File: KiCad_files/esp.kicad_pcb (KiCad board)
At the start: 2 copper layers, 100 x 100 mm, 61 parts, among them J1 Conn_01x08_Socket, J2 USB4105-GF-A, Q2 DMP3099L, SW1 SLW-171175-7A-N-D, U1 B3U-1000P, U12 ESP32-S3-MINI-1U, U13 BNO085, U2 1060, U7 LTC4412xS6

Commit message: gepsiä alotettu
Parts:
- added J3: Conn_01x16_Pin, Connector_PinHeader_2.54mm:PinHeader_1x16_P2.54mm_Vertical, F.Cu at (48.2, 48.5)
- added TP1: BOOT, TestPoint:TestPoint_Pad_D1.0mm, F.Cu at (134.9, 58.9)
- added TP2: JTAG_SOURCE, TestPoint:TestPoint_Pad_D1.0mm, F.Cu at (134.9, 55.4)
- added TP3: VDD_SPI_VOLTAGE, TestPoint:TestPoint_Pad_D1.0mm, F.Cu at (100.0, 60.5)
- added TP4: ROM_PRINTING, TestPoint:TestPoint_Pad_D1.0mm, F.Cu at (100.0, 63.5)
- J1: value Conn_01x08_Socket -> Conn_01x02_Pin; footprint Connector_PinSocket_2.54mm:PinSocket_1x08_P2.54mm_Vertical -> Connector_PinHeader_2.54mm:PinHeader_1x02_P2.54mm_Vertical
- moved J2 79.2 mm to (80.6, 51.3), turned to -90 degrees
- moved R18 57.8 mm to (142.4, 58.6), turned to 90 degrees
- moved R17 57.0 mm to (139.9, 57.4), turned to 90 degrees
- moved C12 54.9 mm to (137.9, 32.3)
- moved C13 54.5 mm to (137.9, 35.8)
- moved C14 54.3 mm to (117.9, 30.1), turned to -90 degrees
- moved R9 50.4 mm to (116.4, 26.3)
- moved L3 48.3 mm to (133.9, 26.3)
- moved U10 43.5 mm to (125.2, 32.1)
- moved J1 42.9 mm to (124.5, 89.8)
- moved C11 42.2 mm to (116.9, 33.3), turned to 180 degrees
- moved C10 36.9 mm to (116.9, 35.8), turned to 180 degrees
- moved U2 36.8 mm to (94.1, 35.8)
- moved L1 36.8 mm to (133.4, 32.6)
- moved L2 36.5 mm to (133.4, 35.6)
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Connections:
- C21 pad 2: +3.3V -> Net-(J1-Pin_1)
- C25 pad 1: +3.3V -> Net-(J1-Pin_1)
- C27 pad 1: +3.3V -> Net-(J1-Pin_1)
- J1 pad 1: GND -> Net-(J1-Pin_1)
- L4 pad 1: +3.3V -> Net-(J1-Pin_1)
- R1 pad 2: +3.3V -> Net-(J1-Pin_1)
- R14 pad 2: +3.3V -> Net-(J1-Pin_1)
- R15 pad 1: +3.3V -> Net-(J1-Pin_1)
- U12 pad 11: unconnected-(U12-IO7-Pad11) -> /BAROMETER_INT
- U12 pad 12: /I2C_SDA -> unconnected-(U12-IO8-Pad12)
- U12 pad 13: /I2C_CLK -> unconnected-(U12-IO9-Pad13)
- U12 pad 14: /BAROMETER_INT -> unconnected-(U12-IO10-Pad14)
- U12 pad 17: /GNSS_FIX -> /GNSS_HW_S
- U12 pad 18: /GNSS_HW_R -> /GNSS_FIX
- U12 pad 19: /GNSS_HW_S -> /GNSS_TM
- U12 pad 20: /GNSS_TM -> /GNSS_HW_R
- U12 pad 30: unconnected-(U12-IO48-Pad30) -> /BAT_STAT
- U12 pad 31: unconnected-(U12-IO35-Pad31) -> /IO35
- U12 pad 32: unconnected-(U12-IO36-Pad32) -> /IO36
- U12 pad 33: unconnected-(U12-IO37-Pad33) -> /IO37
- U12 pad 34: /BAT_STAT -> /IO38
- U12 pad 35: /PWM_0 -> /IO39
- U12 pad 36: /PWM_1 -> /IO40
- U12 pad 37: /PWM_2 -> /IO41
- U12 pad 38: /PWM_3 -> /IO42
- U12 pad 39: unconnected-(U12-TXD0-Pad39) -> /IO43
- U12 pad 4: unconnected-(U12-IO0-Pad4) -> Net-(U12-IO0)
- U12 pad 40: unconnected-(U12-RXD0-Pad40) -> /IO44
- U12 pad 41: unconnected-(U12-IO45-Pad41) -> Net-(U12-IO45)
- U12 pad 44: unconnected-(U12-IO46-Pad44) -> Net-(U12-IO46)
- U12 pad 5: unconnected-(U12-IO1-Pad5) -> /I2C_SDA
- U12 pad 6: unconnected-(U12-IO2-Pad6) -> /I2C_CLK
- U12 pad 7: /JTAG_SEL -> Net-(U12-IO3)
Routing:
- net GND: track 30.4 -> 69.7 mm
- net /GNSS_HW_S: track 0.00 -> 37.7 mm
- net /GNSS_RX: track 0.00 -> 30.5 mm
- net /GNSS_TX: track 0.00 -> 20.6 mm
- net /GNSS_HW_R: track 0.00 -> 20.1 mm, vias 0 -> 2
- net +3.3V: track 63.7 -> 83.7 mm
- net /GNSS_TM: track 0.00 -> 18.3 mm, vias 0 -> 2
- net /I2C_SDA: track 10.5 -> 24.5 mm
- net /I2C_CLK: track 10.3 -> 22.0 mm
- net /GNSS_FIX: track 0.00 -> 11.3 mm, vias 0 -> 2
- net /USB_D-: track 0.00 -> 9.01 mm
- net Net-(U10-BV): track 0.00 -> 8.06 mm, vias 0 -> 2
- net /USB_D+: track 0.00 -> 7.96 mm
- net Net-(U10-AT1): track 0.00 -> 3.66 mm
- net Net-(U10-AT2): track 0.00 -> 3.51 mm
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- removed copper zone on F.Cu, net GND

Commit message: wippistä
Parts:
- removed R2: 10K, Resistor_SMD:R_0805_2012Metric_Pad1.20x1.40mm_HandSolder
- moved R7 73.4 mm to (98.5, 32.2)
- moved R6 67.8 mm to (93.7, 39.3)
- moved J3 59.2 mm to (107.0, 41.6)
- moved C8 47.2 mm to (135.4, 62.2), turned to -90 degrees
- moved C7 44.5 mm to (137.9, 62.2), turned to -90 degrees
- moved R8 43.8 mm to (120.0, 66.0), turned to -90 degrees
- moved C6 40.4 mm to (117.0, 66.0), turned to -90 degrees
- moved U1 39.2 mm to (125.0, 66.0), turned to 180 degrees
- moved C15 26.6 mm to (161.8, 59.5)
- moved C16 26.2 mm to (161.8, 63.0)
- moved U2 25.7 mm to (89.8, 61.1), turned to 90 degrees
- moved J2 15.2 mm to (81.2, 36.1)
- moved TP4 15.1 mm to (115.0, 62.0)
- moved TP3 15.0 mm to (115.0, 59.8)
- moved U11 7.42 mm to (153.8, 60.7)
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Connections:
- J3 pad 1: GND -> /IO35
- J3 pad 10: /IO38 -> /IO44
- J3 pad 11: /IO39 -> GND
- J3 pad 12: /IO40 -> GND
- J3 pad 13: /IO41 -> /BAT
- J3 pad 14: /IO42 -> /BAT
- J3 pad 15: /IO43 -> +3.3V
- J3 pad 16: /IO44 -> +3.3V
- J3 pad 2: GND -> /IO36
- J3 pad 3: /BAT -> /IO37
- J3 pad 4: /BAT -> /IO38
- J3 pad 5: +3.3V -> /IO39
- J3 pad 6: +3.3V -> /IO40
- J3 pad 7: /IO35 -> /IO41
- J3 pad 8: /IO36 -> /IO42
- J3 pad 9: /IO37 -> /IO43
- U12 pad 18: /GNSS_FIX -> /GNSS_RX
- U12 pad 19: /GNSS_TM -> /GNSS_TX
- U12 pad 20: /GNSS_HW_R -> /GNSS_FIX
- U12 pad 21: /GNSS_RX -> /GNSS_TM
- U12 pad 22: /GNSS_TX -> /GNSS_HW_R
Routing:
- net GND: track 69.7 -> 30.4 mm
- net +3.3V: track 83.7 -> 112.9 mm
- net /BAT_STAT: track 2.65 -> 19.5 mm
- net /IO44: track 0.00 -> 16.4 mm
- net /IO43: track 0.00 -> 14.5 mm
- net /I2C_SDA: track 24.5 -> 10.1 mm
- net /IO35: track 0.00 -> 14.1 mm
- net /USB_D+: track 7.96 -> 22.0 mm
- net /USB_D-: track 9.01 -> 22.7 mm
- net /IO36: track 0.00 -> 13.4 mm
- net /IO42: track 0.00 -> 12.8 mm
- net /IO37: track 0.00 -> 12.7 mm
- net /IO41: track 0.00 -> 12.1 mm
- net /I2C_CLK: track 22.0 -> 9.93 mm
- net /IO38: track 0.00 -> 12.0 mm
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
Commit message: wip
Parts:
- added REF**: MountingHole_3mm, MountingHole:MountingHole_3mm, F.Cu at (85.2, 28.2)
- added REF**: MountingHole_3mm, MountingHole:MountingHole_3mm, F.Cu at (164.8, 28.2)
- added REF**: MountingHole_3mm, MountingHole:MountingHole_3mm, F.Cu at (85.2, 96.8)
- added REF**: MountingHole_3mm, MountingHole:MountingHole_3mm, F.Cu at (164.8, 96.8)
- moved D1 40.1 mm to (155.7, 87.9)
- moved D3 40.1 mm to (155.5, 90.9)
- moved Q2 40.1 mm to (155.8, 84.2)
- moved C18 40.1 mm to (144.9, 86.5)
- moved C19 40.1 mm to (144.9, 89.5)
- moved C21 40.1 mm to (144.9, 95.5)
- moved C25 40.1 mm to (150.3, 87.0)
- moved C26 40.1 mm to (150.3, 90.3)
- moved D2 40.1 mm to (149.9, 96.8)
- moved J1 40.1 mm to (161.2, 74.1)
- moved L4 40.1 mm to (148.7, 76.0)
- moved R11 40.1 mm to (140.1, 77.4)
- moved R12 40.1 mm to (140.1, 80.3)
- moved R13 40.1 mm to (140.1, 83.3)
- moved U8 40.1 mm to (130.9, 96.7)
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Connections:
- U12 pad 11: /BAROMETER_INT -> unconnected-(U12-IO7-Pad11)
- U12 pad 16: unconnected-(U12-IO12-Pad16) -> /BAROMETER_INT
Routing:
- net +3.3V: track 112.9 -> 196.2 mm, vias 0 -> 2
- net Net-(U10-BV): track 3.39 -> 64.8 mm, vias 0 -> 4
- net /USB_VBUS: track 0.00 -> 59.4 mm
- net /USB_D-: track 22.7 -> 42.9 mm
- net /USB_D+: track 22.0 -> 41.9 mm
- net /BAT_STAT: track 19.5 -> 0.00 mm
- net /I2C_SDA: track 10.1 -> 25.0 mm
- net /I2C_CLK: track 9.93 -> 22.4 mm
- net Net-(U12-EN): track 0.00 -> 12.2 mm
- net Net-(J2-CC1): track 0.00 -> 5.57 mm
- net Net-(J2-CC2): track 0.00 -> 5.37 mm
- net Net-(U12-IO3): track 0.00 -> 3.75 mm
- net Net-(U12-IO0): track 0.00 -> 3.75 mm
- net /BAROMETER_INT: track 0.00 -> 3.06 mm
- net Net-(U12-IO46): track 3.79 -> 4.73 mm
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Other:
- board size 100 x 100 mm -> 86 x 75 mm

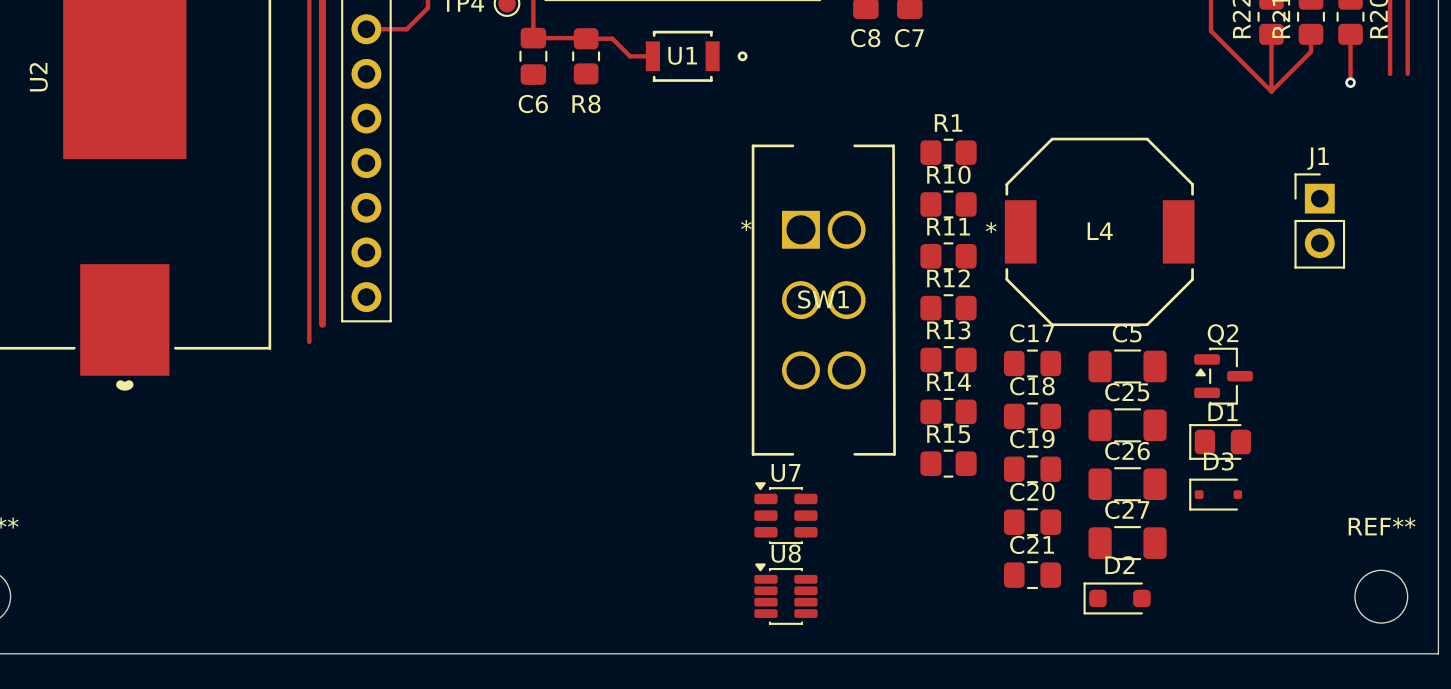
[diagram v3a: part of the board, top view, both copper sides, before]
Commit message: power supply to pcb
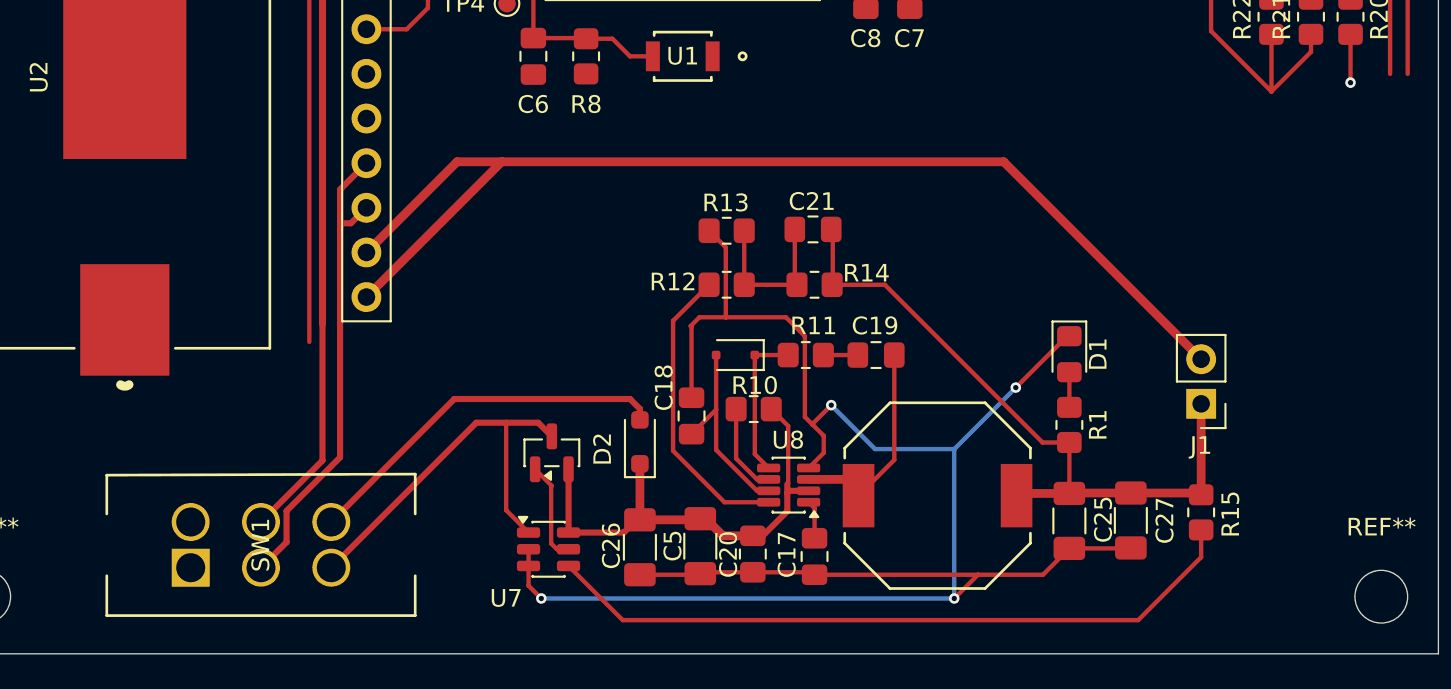
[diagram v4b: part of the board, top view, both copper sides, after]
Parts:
- moved SW1 39.7 mm to (97.0, 95.1), turned to 90 degrees
- moved Q2 38.5 mm to (117.5, 88.6), turned to 90 degrees
- moved D2 28.7 mm to (122.6, 87.9), turned to 90 degrees
- moved D3 28.6 mm to (128.0, 83.0), turned to 180 degrees
- moved C26 28.0 mm to (122.6, 93.9), turned to -90 degrees
- moved C5 26.4 mm to (126.0, 93.9), turned to -90 degrees
- moved C21 23.3 mm to (132.4, 75.8)
- moved C18 19.4 mm to (125.5, 86.5), turned to -90 degrees
- moved L4 17.6 mm to (139.5, 91.0), turned to 180 degrees
- moved R1 17.0 mm to (147.0, 87.0), turned to -90 degrees
- moved C17 16.6 mm to (132.5, 94.5), turned to 90 degrees
- moved R10 16.1 mm to (129.0, 86.1)
- moved C20 16.0 mm to (129.0, 94.3), turned to 90 degrees
- moved R15 14.6 mm to (154.5, 92.0), turned to -90 degrees
- moved R13 14.6 mm to (127.5, 75.9)
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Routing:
- net GND: track 30.4 -> 139.3 mm, vias 5 -> 9
- net +3.3V: track 196.2 -> 261.4 mm
- net /BAT_STAT: track 0.00 -> 40.3 mm
- net Net-(J1-Pin_1): track 0.00 -> 38.2 mm
- net Net-(D2-K): track 0.00 -> 27.5 mm
- net /BAT: track 0.00 -> 27.4 mm
- net Net-(Q2-D): track 0.00 -> 23.1 mm
- net Net-(D2-A): track 0.00 -> 21.3 mm
- net Net-(R12-Pad1): track 0.00 -> 16.9 mm
- net /USB_VBUS: track 59.4 -> 72.1 mm
- net Net-(D3-A): track 0.00 -> 11.3 mm
- net Net-(U8-SW): track 0.00 -> 10.8 mm
- net Net-(C21-Pad1): track 0.00 -> 9.10 mm
- net Net-(D3-K): track 0.00 -> 8.65 mm
- net Net-(Q2-G): track 0.00 -> 5.74 mm
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
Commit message: liitoksia
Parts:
- moved C15 2.99 mm to (153.0, 35.0)
- moved C22 2.88 mm to (162.4, 48.8)
- moved C23 2.88 mm to (159.9, 48.7)
- moved C24 2.88 mm to (153.1, 54.0)
- moved R16 2.88 mm to (154.9, 48.8)
- moved R20 2.88 mm to (160.1, 63.8)
- moved R21 2.88 mm to (157.9, 63.8)
- moved R22 2.88 mm to (155.6, 63.8)
- moved R23 2.88 mm to (153.2, 57.2)
- moved U13 2.88 mm to (159.4, 55.8)
- moved U11 2.51 mm to (153.5, 39.2)
- moved C16 2.25 mm to (156.0, 35.0)
- moved TP2 0.75 mm to (135.5, 56.0)
- moved TP1 0.50 mm to (135.5, 58.5)
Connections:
- U12 pad 10: /IMU_BOOTN -> /IMU_NRST
- U12 pad 11: unconnected-(U12-IO7-Pad11) -> /IMU_BOOTN
- U12 pad 12: unconnected-(U12-IO8-Pad12) -> /I2C_SDA
- U12 pad 13: unconnected-(U12-IO9-Pad13) -> /I2C_CLK
- U12 pad 14: unconnected-(U12-IO10-Pad14) -> /BAROMETER_INT
- U12 pad 16: /BAROMETER_INT -> /BAT_STAT
- U12 pad 30: /BAT_STAT -> unconnected-(U12-IO48-Pad30)
- U12 pad 5: /I2C_SDA -> unconnected-(U12-IO1-Pad5)
- U12 pad 6: /I2C_CLK -> unconnected-(U12-IO2-Pad6)
- U12 pad 8: /IMU_INT -> unconnected-(U12-IO4-Pad8)
- U12 pad 9: /IMU_NRST -> /IMU_INT
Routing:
- net /BAT_STAT: track 40.3 -> 150.4 mm
- net /I2C_CLK: track 22.4 -> 78.4 mm
- net /I2C_SDA: track 25.0 -> 78.3 mm, vias 0 -> 2
- net /BAROMETER_INT: track 3.06 -> 28.5 mm
- net /IMU_NRST: track 15.5 -> 30.3 mm
- net /IMU_BOOTN: track 17.8 -> 32.4 mm
- net /IMU_INT: track 16.6 -> 31.2 mm
- net +3.3V: track 261.4 -> 257.4 mm

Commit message: liitoksia
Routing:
- net +3.3V: track 257.4 -> 315.1 mm
- net GND: track 139.3 -> 138.2 mm
- net /I2C_SDA: track 78.3 -> 77.5 mm
